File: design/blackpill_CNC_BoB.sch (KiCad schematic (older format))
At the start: 299 parts, among them J101 ALimIN, J102 ZLimIN, J103 YLimIN, J104 XLimIN, J105 CS_IN, J106 FH_IN, J107 DoorIN, J108 ResetIN, J109 ProbeIN, J110 12V Power in, J111 AuxEncIn, J112 5V Power out, J113 ADC_in_1, J114 ADC_in_2, J115 stepDriverLim, J116 Reset, J117 UART1, J118 I2C, J119 SpindleVFD, J120 Spindle/Coolant, J121 Spindle, J122 Coolant, J123 AuxOut, J124 XStepDrv, J125 YStepDrv, J126 ZStepDrv, J127 AStepDrv, U101 TLP290-4, U102 TLP290-4, U103 TLP290-4, U104 74LVC2G17, U105 LD1117S50TR_SOT223, U106 LM358, U107 TLV9001, U108 TLV9001, U109 YAAJ_WeAct_BlackPill_Part_Like, U110 TLV9001, U111 TLV9001, U112 74HCT541, U113 74HCT541, U114 74HCT541, U115 ULN2003A, U116 ULN2003A, U117 ULN2003A

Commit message: place buffer cercos
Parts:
- added C124, C125, C126: 100nF, Capacitor_SMD:C_0603_1608Metric, symbol Device:C
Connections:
- net +5V: now also C125.1
- net GND: now also C124.2, C125.2, C126.2
- net UADCdriver: now also C124.1, C126.1
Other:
- moved on the sheet: C108, C109, C110, C113, JP112
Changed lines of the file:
@@
-$EndComp
-$Comp
-L power:GND #PWR0118
-U 1 1 7569D2D7
-P 4700 10700
-F 0 "#PWR0118" H 4700 10450 50  0001 C CNN
-F 1 "GND" H 4750 10500 50  0001 C CNN
-F 2 "" H 4700 10700 50  0001 C CNN
-F 3 "" H 4700 10700 50  0001 C CNN
-	1    4700 10700
-	1    0    0    -1
-$EndComp
-$Comp
-L Device:C C108
-U 1 1 7569D2E3
-P 4550 10400
-F 0 "C108" H 4600 10300 50  0000 L CNN
-F 1 "100nF" H 4450 10500 50  0000 L CNN
-F 2 "Capacitor_SMD:C_0603_1608Metric" H 4588 10250 50  0001 C CNN
-F 3 "~" H 4550 10400 50  0001 C CNN
-	1    4550 10400
-	1    0    0    -1
-$EndComp
-Wire Wire Line
-	4550 10100 4550 10250
-Wire Wire Line
-	4550 10550 4550 10700
-Wire Wire Line
-	4550 10700 4700 10700
-Wire Wire Line
-	4700 10700 4850 10700
-Connection ~ 4700 10700
-$Comp
-L power:GND #PWR0127
-U 1 1 756F2E58
-P 5450 10700
-F 0 "#PWR0127" H 5450 10450 50  0001 C CNN
-F 1 "GND" H 5500 10500 50  0001 C CNN
-F 2 "" H 5450 10700 50  0001 C CNN
-F 3 "" H 5450 10700 50  0001 C CNN
-	1    5450 10700
-	1    0    0    -1
-$EndComp
-$Comp
-L Device:C C110
-U 1 1 756F2E64
-P 5300 10400
-F 0 "C110" H 5350 10300 50  0000 L CNN
-F 1 "100nF" H 5200 10500 50  0000 L CNN
-F 2 "Capacitor_SMD:C_0603_1608Metric" H 5338 10250 50  0001 C CNN
-F 3 "~" H 5300 10400 50  0001 C CNN
-	1    5300 10400
-	1    0    0    -1
-$EndComp
-Wire Wire Line
-	5300 10100 5300 10250
-Wire Wire Line
-	5300 10550 5300 10700
-Wire Wire Line
-	5300 10700 5450 10700
-Wire Wire Line
-	5450 10700 5600 10700
-Connection ~ 5450 10700
-Wire Wire Line
-	4550 10100 4700 10100
-$Comp
-L power:+5V #PWR0117
-U 1 1 73BC8B53
-P 4700 10100
-F 0 "#PWR0117" H 4700 9950 50  0001 C CNN
-F 1 "+5V" H 4750 10300 50  0001 C CNN
-F 2 "" H 4700 10100 50  0001 C CNN
-F 3 "" H 4700 10100 50  0001 C CNN
-	1    4700 10100
-	1    0    0    -1
-$EndComp
-Connection ~ 4700 10100
-Wire Wire Line
-	4700 10100 4850 10100
-$Comp
-L power:+5V #PWR0125
-U 1 1 758539CE
-P 5350 9500
-F 0 "#PWR0125" H 5350 9350 50  0001 C CNN
-F 1 "+5V" H 5400 9700 50  0001 C CNN
-F 2 "" H 5350 9500 50  0001 C CNN
-F 3 "" H 5350 9500 50  0001 C CNN
-	1    5350 9500
-	0    -1   -1   0
 $EndComp
 $Comp
@@
 Text Label 8150 4600 0    50   ~ 0
 UADCdriver
-$Comp
-L Device:C C109
-U 1 1 768A9165
-P 4850 10400
-F 0 "C109" H 4900 10300 50  0000 L CNN
-F 1 "100nF" H 4750 10500 50  0000 L CNN
-F 2 "Capacitor_SMD:C_0603_1608Metric" H 4888 10250 50  0001 C CNN
-F 3 "~" H 4850 10400 50  0001 C CNN
-	1    4850 10400
-	1    0    0    -1
-$EndComp
-$Comp
-L Device:C C113
-U 1 1 768A9343
-P 5600 10400
-F 0 "C113" H 5650 10300 50  0000 L CNN
-F 1 "100nF" H 5500 10500 50  0000 L CNN
-F 2 "Capacitor_SMD:C_0603_1608Metric" H 5638 10250 50  0001 C CNN
-F 3 "~" H 5600 10400 50  0001 C CNN
-	1    5600 10400
-	1    0    0    -1
-$EndComp
-$Comp
-L power:+3.3V #PWR0126
-U 1 1 768B85AD
-P 5350 10000
-F 0 "#PWR0126" H 5350 9850 50  0001 C CNN
-F 1 "+3.3V" H 5365 10173 50  0001 C CNN
-F 2 "" H 5350 10000 50  0001 C CNN
-F 3 "" H 5350 10000 50  0001 C CNN
-	1    5350 10000
-	0    -1   -1   0
-$EndComp
 Text Label 10700 9600 1    50   ~ 0
 UADCdriver
-Wire Wire Line
-	4850 10100 4850 10250
-Wire Wire Line
-	4850 10550 4850 10700
-Wire Wire Line
-	5600 10700 5600 10550
-Wire Wire Line
-	5600 10100 5600 10250
-$Comp
-L Device:Jumper_NC_Dual JP112
-U 1 1 76A11CC6
-P 5350 9750
-F 0 "JP112" H 5350 9900 50  0000 L CNN
-F 1 "Jumper_NC_Dual" V 5350 9900 50  0001 L CNN
-F 2 "Connector_PinHeader_2.54mm:PinHeader_1x03_P2.54mm_Vertical" H 5350 9750 50  0001 C CNN
-F 3 "~" H 5350 9750 50  0001 C CNN
-	1    5350 9750
-	0    -1   -1   0
-$EndComp
-Wire Wire Line
-	5300 10100 5600 10100
-Connection ~ 5600 10100
-Wire Wire Line
-	5600 9700 5600 9750
-Wire Wire Line
-	5450 9750 5600 9750
-Connection ~ 5600 9750
-Wire Wire Line
-	5600 9750 5600 10100
 $Comp
 L Device:R R141
@@
 Wire Wire Line
 	2900 10850 3050 10850
-Text Label 5600 9700 0    50   ~ 0
-UADCdriver
 $Comp
 L Diode:1N5819 D120
@@
 Wire Wire Line
 	6240 2980 6110 2980
+Text Label 4800 8900 0    50   ~ 0
+UADCdriver
+Wire Wire Line
+	4800 8950 4800 9300
+Connection ~ 4800 8950
+Wire Wire Line
+	4650 8950 4800 8950
+Wire Wire Line
+	4800 8900 4800 8950
+Connection ~ 4800 9300
+Wire Wire Line
+	4500 9300 4800 9300
+$Comp
+L Device:Jumper_NC_Dual JP112
+U 1 1 76A11CC6
+P 4550 8950
+F 0 "JP112" H 4550 9100 50  0000 L CNN
+F 1 "Jumper_NC_Dual" V 4550 9100 50  0001 L CNN
+F 2 "Connector_PinHeader_2.54mm:PinHeader_1x03_P2.54mm_Vertical" H 4550 8950 50  0001 C CNN
+F 3 "~" H 4550 8950 50  0001 C CNN
+	1    4550 8950
+	0    -1   -1   0
+$EndComp
+Wire Wire Line
+	4800 9300 4800 9450
+Wire Wire Line
+	4800 9900 4800 9750
+$Comp
+L power:+3.3V #PWR0126
+U 1 1 768B85AD
+P 4550 9200
+F 0 "#PWR0126" H 4550 9050 50  0001 C CNN
+F 1 "+3.3V" H 4565 9373 50  0001 C CNN
+F 2 "" H 4550 9200 50  0001 C CNN
+F 3 "" H 4550 9200 50  0001 C CNN
+	1    4550 9200
+	0    -1   -1   0
+$EndComp
+$Comp
+L Device:C C113
+U 1 1 768A9343
+P 4800 9600
+F 0 "C113" H 4850 9500 50  0000 L CNN
+F 1 "100nF" H 4700 9700 50  0000 L CNN
+F 2 "Capacitor_SMD:C_0603_1608Metric" H 4838 9450 50  0001 C CNN
+F 3 "~" H 4800 9600 50  0001 C CNN
+	1    4800 9600
+	1    0    0    -1
+$EndComp
+$Comp
+L power:+5V #PWR0125
+U 1 1 758539CE
+P 4550 8700
+F 0 "#PWR0125" H 4550 8550 50  0001 C CNN
+F 1 "+5V" H 4600 8900 50  0001 C CNN
+F 2 "" H 4550 8700 50  0001 C CNN
+F 3 "" H 4550 8700 50  0001 C CNN
+	1    4550 8700
+	0    -1   -1   0
+$EndComp
+Connection ~ 4650 9900
+Wire Wire Line
+	4650 9900 4800 9900
+Wire Wire Line
+	4500 9900 4650 9900
+Wire Wire Line
+	4500 9750 4500 9900
+Wire Wire Line
+	4500 9300 4500 9450
+$Comp
+L Device:C C110
+U 1 1 756F2E64
+P 4500 9600
+F 0 "C110" H 4550 9500 50  0000 L CNN
+F 1 "100nF" H 4400 9700 50  0000 L CNN
+F 2 "Capacitor_SMD:C_0603_1608Metric" H 4538 9450 50  0001 C CNN
+F 3 "~" H 4500 9600 50  0001 C CNN
+	1    4500 9600
+	1    0    0    -1
+$EndComp
+$Comp
+L power:GND #PWR0127
+U 1 1 756F2E58
+P 4650 9900
+F 0 "#PWR0127" H 4650 9650 50  0001 C CNN
+F 1 "GND" H 4700 9700 50  0001 C CNN
+F 2 "" H 4650 9900 50  0001 C CNN
+F 3 "" H 4650 9900 50  0001 C CNN
+	1    4650 9900
+	1    0    0    -1
+$EndComp
+Wire Wire Line
+	4850 10750 4850 10900
+Wire Wire Line
+	4850 10300 4850 10450
+$Comp
+L Device:C C109
+U 1 1 768A9165
+P 4850 10600
+F 0 "C109" H 4900 10500 50  0000 L CNN
+F 1 "100nF" H 4750 10700 50  0000 L CNN
+F 2 "Capacitor_SMD:C_0603_1608Metric" H 4888 10450 50  0001 C CNN
+F 3 "~" H 4850 10600 50  0001 C CNN
+	1    4850 10600
+	1    0    0    -1
+$EndComp
+Wire Wire Line
+	4700 10300 4850 10300
+Connection ~ 4700 10300
+$Comp
+L power:+5V #PWR0117
+U 1 1 73BC8B53
+P 4700 10300
+F 0 "#PWR0117" H 4700 10150 50  0001 C CNN
+F 1 "+5V" H 4750 10500 50  0001 C CNN
+F 2 "" H 4700 10300 50  0001 C CNN
+F 3 "" H 4700 10300 50  0001 C CNN
+	1    4700 10300
+	1    0    0    -1
+$EndComp
+Wire Wire Line
+	4550 10300 4700 10300
+Connection ~ 4700 10900
+Wire Wire Line
+	4700 10900 4850 10900
+Wire Wire Line
+	4550 10900 4700 10900
+Wire Wire Line
+	4550 10750 4550 10900
+Wire Wire Line
+	4550 10300 4550 10450
+$Comp
+L Device:C C108
+U 1 1 7569D2E3
+P 4550 10600
+F 0 "C108" H 4600 10500 50  0000 L CNN
+F 1 "100nF" H 4450 10700 50  0000 L CNN
+F 2 "Capacitor_SMD:C_0603_1608Metric" H 4588 10450 50  0001 C CNN
+F 3 "~" H 4550 10600 50  0001 C CNN
+	1    4550 10600
+	1    0    0    -1
+$EndComp
+$Comp
+L power:GND #PWR0118
+U 1 1 7569D2D7
+P 4700 10900
+F 0 "#PWR0118" H 4700 10650 50  0001 C CNN
+F 1 "GND" H 4750 10700 50  0001 C CNN
+F 2 "" H 4700 10900 50  0001 C CNN
+F 3 "" H 4700 10900 50  0001 C CNN
+	1    4700 10900
+	1    0    0    -1
+$EndComp
+$Comp
+L Device:C C125
+U 1 1 68D74ED4
+P 5100 10600
+F 0 "C125" H 5150 10500 50  0000 L CNN
+F 1 "100nF" H 5000 10700 50  0000 L CNN
+F 2 "Capacitor_SMD:C_0603_1608Metric" H 5138 10450 50  0001 C CNN
+F 3 "~" H 5100 10600 50  0001 C CNN
+	1    5100 10600
+	1    0    0    -1
+$EndComp
+$Comp
+L Device:C C124
+U 1 1 68E10737
+P 5100 9600
+F 0 "C124" H 5150 9500 50  0000 L CNN
+F 1 "100nF" H 5000 9700 50  0000 L CNN
+F 2 "Capacitor_SMD:C_0603_1608Metric" H 5138 9450 50  0001 C CNN
+F 3 "~" H 5100 9600 50  0001 C CNN
+	1    5100 9600
+	1    0    0    -1
+$EndComp
+$Comp
+L Device:C C126
+U 1 1 68E11AD2
+P 5400 9600
+F 0 "C126" H 5450 9500 50  0000 L CNN
+F 1 "100nF" H 5300 9700 50  0000 L CNN
+F 2 "Capacitor_SMD:C_0603_1608Metric" H 5438 9450 50  0001 C CNN
+F 3 "~" H 5400 9600 50  0001 C CNN
+	1    5400 9600
+	1    0    0    -1
+$EndComp
+Wire Wire Line
+	4850 10300 5100 10300
+Wire Wire Line
+	5100 10300 5100 10450
+Connection ~ 4850 10300
+Wire Wire Line
+	4850 10900 5100 10900
+Wire Wire Line
+	5100 10900 5100 10750
+Connection ~ 4850 10900
+Wire Wire Line
+	4800 9900 5100 9900
+Wire Wire Line
+	5400 9900 5400 9750
+Connection ~ 4800 9900
+Wire Wire Line
+	5100 9750 5100 9900
+Connection ~ 5100 9900
+Wire Wire Line
+	5100 9900 5400 9900
+Wire Wire Line
+	4800 9300 5100 9300
+Wire Wire Line
+	5400 9300 5400 9450
+Wire Wire Line
+	5100 9450 5100 9300
+Connection ~ 5100 9300
+Wire Wire Line
+	5100 9300 5400 9300
 $EndSCHEMATC

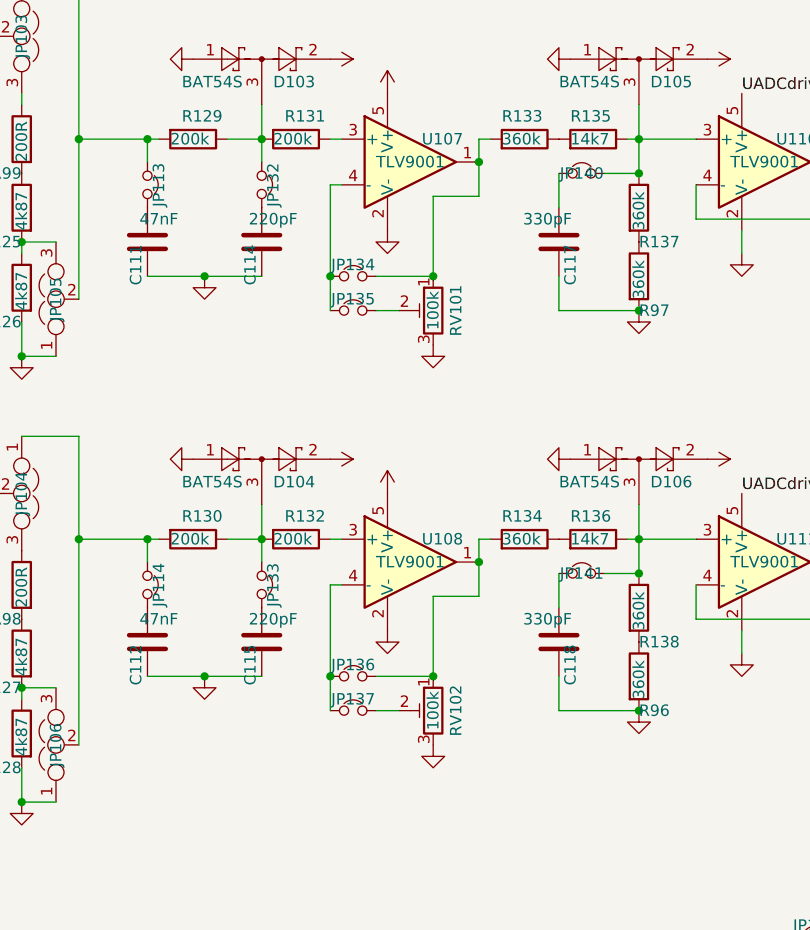
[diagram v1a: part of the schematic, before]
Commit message: refigure AD in jumper
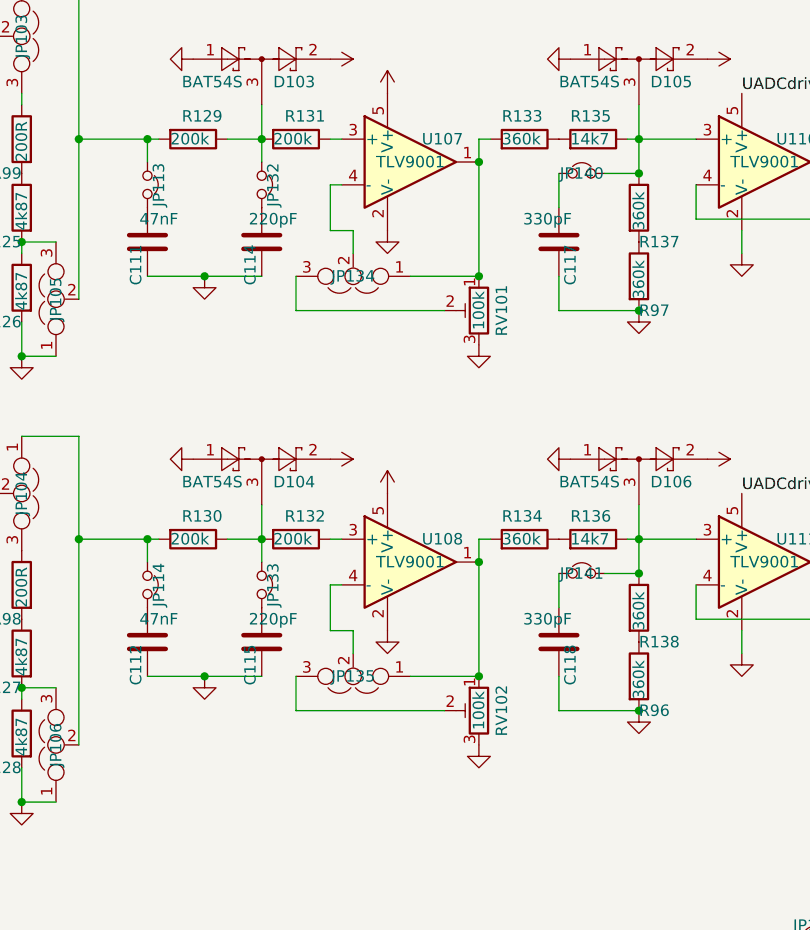
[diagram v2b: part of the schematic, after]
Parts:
- removed JP134, JP135, JP136, JP137: Jumper_NC_Small, Connector_PinHeader_2.54mm:PinHeader_1x02_P2.54mm_Vertical, symbol Device:Jumper_NC_Small
- added JP134, JP135: Jumper_NC_Dual, Connector_PinHeader_2.54mm:PinHeader_1x03_P2.54mm_Vertical, symbol Device:Jumper_NC_Dual
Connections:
- net at R133.2, RV101.1, U107.1: now also JP134.1
- net at RV101.2: now also JP134.3
- net at U107.4 (-): now also JP134.2
- net at R134.2, RV102.1, U108.1: now also JP135.1
- net at RV102.2: now also JP135.3
- net at U108.4 (-): now also JP135.2
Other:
- moved on the sheet: RV101, RV102
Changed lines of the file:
@@
 L Device:R_POT_TRIM RV101
 U 1 1 74D34F66
-P 6800 5550
-F 0 "RV101" V 6700 5550 50  0000 C CNN
-F 1 "100k" V 6800 5550 50  0000 C CNN
-F 2 "Potentiometer_THT:Potentiometer_Bourns_3296W_Vertical" H 6800 5550 50  0001 C CNN
-F 3 "~" H 6800 5550 50  0001 C CNN
-	1    6800 5550
+P 7000 5550
+F 0 "RV101" V 6900 5550 50  0000 C CNN
+F 1 "100k" V 7000 5550 50  0000 C CNN
+F 2 "Potentiometer_THT:Potentiometer_Bourns_3296W_Vertical" H 7000 5550 50  0001 C CNN
+F 3 "~" H 7000 5550 50  0001 C CNN
+	1    7000 5550
 	-1   0    0    -1
 $EndComp
@@
 L power:GNDS #PWR0143
 U 1 1 74FB2393
-P 6800 5700
-F 0 "#PWR0143" H 6800 5450 50  0001 C CNN
-F 1 "GNDS" H 6805 5527 50  0001 C CNN
-F 2 "" H 6800 5700 50  0001 C CNN
-F 3 "" H 6800 5700 50  0001 C CNN
-	1    6800 5700
-	1    0    0    -1
-$EndComp
-$Comp
-L Device:Jumper_NC_Small JP135
-U 1 1 74FB28D6
-P 6450 5550
-F 0 "JP135" H 6450 5600 50  0000 C CNN
-F 1 "Jumper_NC_Small" H 6450 5700 50  0001 C CNN
-F 2 "Connector_PinHeader_2.54mm:PinHeader_1x02_P2.54mm_Vertical" H 6450 5550 50  0001 C CNN
-F 3 "~" H 6450 5550 50  0001 C CNN
-	1    6450 5550
-	-1   0    0    -1
-$EndComp
-$Comp
-L Device:Jumper_NC_Small JP134
-U 1 1 74FB2AFA
-P 6450 5400
-F 0 "JP134" H 6450 5450 50  0000 C CNN
-F 1 "Jumper_NC_Small" H 6450 5550 50  0001 C CNN
-F 2 "Connector_PinHeader_2.54mm:PinHeader_1x02_P2.54mm_Vertical" H 6450 5400 50  0001 C CNN
-F 3 "~" H 6450 5400 50  0001 C CNN
-	1    6450 5400
-	-1   0    0    -1
+P 7000 5700
+F 0 "#PWR0143" H 7000 5450 50  0001 C CNN
+F 1 "GNDS" H 7005 5527 50  0001 C CNN
+F 2 "" H 7000 5700 50  0001 C CNN
+F 3 "" H 7000 5700 50  0001 C CNN
+	1    7000 5700
+	1    0    0    -1
 $EndComp
 $Comp
@@
 $EndComp
 Wire Wire Line
-	6350 5550 6350 5400
-Wire Wire Line
 	6350 5000 6400 5000
-Connection ~ 6350 5400
-Wire Wire Line
-	6350 5400 6350 5000
-Wire Wire Line
-	6550 5400 6800 5400
-Wire Wire Line
-	6650 5550 6550 5550
-Wire Wire Line
-	7000 4900 7000 5050
-Wire Wire Line
-	7000 5050 6800 5050
-Wire Wire Line
-	6800 5050 6800 5400
-Connection ~ 6800 5400
 $Comp
 L Device:R R135
@@
 L Device:R_POT_TRIM RV102
 U 1 1 77513692
-P 6800 7300
-F 0 "RV102" V 6700 7300 50  0000 C CNN
-F 1 "100k" V 6800 7300 50  0000 C CNN
-F 2 "Potentiometer_THT:Potentiometer_Bourns_3296W_Vertical" H 6800 7300 50  0001 C CNN
-F 3 "~" H 6800 7300 50  0001 C CNN
-	1    6800 7300
+P 7000 7300
+F 0 "RV102" V 6900 7300 50  0000 C CNN
+F 1 "100k" V 7000 7300 50  0000 C CNN
+F 2 "Potentiometer_THT:Potentiometer_Bourns_3296W_Vertical" H 7000 7300 50  0001 C CNN
+F 3 "~" H 7000 7300 50  0001 C CNN
+	1    7000 7300
 	-1   0    0    -1
 $EndComp
@@
 L power:GNDS #PWR0144
 U 1 1 77513698
-P 6800 7450
-F 0 "#PWR0144" H 6800 7200 50  0001 C CNN
-F 1 "GNDS" H 6805 7277 50  0001 C CNN
-F 2 "" H 6800 7450 50  0001 C CNN
-F 3 "" H 6800 7450 50  0001 C CNN
-	1    6800 7450
-	1    0    0    -1
-$EndComp
-$Comp
-L Device:Jumper_NC_Small JP137
-U 1 1 7751369E
-P 6450 7300
-F 0 "JP137" H 6450 7350 50  0000 C CNN
-F 1 "Jumper_NC_Small" H 6450 7450 50  0001 C CNN
-F 2 "Connector_PinHeader_2.54mm:PinHeader_1x02_P2.54mm_Vertical" H 6450 7300 50  0001 C CNN
-F 3 "~" H 6450 7300 50  0001 C CNN
-	1    6450 7300
-	-1   0    0    -1
-$EndComp
-$Comp
-L Device:Jumper_NC_Small JP136
-U 1 1 775136A4
-P 6450 7150
-F 0 "JP136" H 6450 7200 50  0000 C CNN
-F 1 "Jumper_NC_Small" H 6450 7300 50  0001 C CNN
-F 2 "Connector_PinHeader_2.54mm:PinHeader_1x02_P2.54mm_Vertical" H 6450 7150 50  0001 C CNN
-F 3 "~" H 6450 7150 50  0001 C CNN
-	1    6450 7150
-	-1   0    0    -1
+P 7000 7450
+F 0 "#PWR0144" H 7000 7200 50  0001 C CNN
+F 1 "GNDS" H 7005 7277 50  0001 C CNN
+F 2 "" H 7000 7450 50  0001 C CNN
+F 3 "" H 7000 7450 50  0001 C CNN
+	1    7000 7450
+	1    0    0    -1
 $EndComp
 $Comp
@@
 $EndComp
 Wire Wire Line
-	6350 7300 6350 7150
-Wire Wire Line
 	6350 6750 6400 6750
-Connection ~ 6350 7150
-Wire Wire Line
-	6350 7150 6350 6750
-Wire Wire Line
-	6550 7150 6800 7150
-Wire Wire Line
-	6650 7300 6550 7300
-Wire Wire Line
-	7000 6650 7000 6800
-Wire Wire Line
-	7000 6800 6800 6800
-Wire Wire Line
-	6800 6800 6800 7150
-Connection ~ 6800 7150
 $Comp
 L Device:R R136
@@
 Wire Wire Line
 	5100 9300 5400 9300
+$Comp
+L Device:Jumper_NC_Dual JP135
+U 1 1 6913274A
+P 6450 7150
+F 0 "JP135" H 6450 7150 50  0000 C CNN
+F 1 "Jumper_NC_Dual" H 6450 7350 50  0001 C CNN
+F 2 "Connector_PinHeader_2.54mm:PinHeader_1x03_P2.54mm_Vertical" H 6450 7150 50  0001 C CNN
+F 3 "~" H 6450 7150 50  0001 C CNN
+	1    6450 7150
+	-1   0    0    1
+$EndComp
+$Comp
+L Device:Jumper_NC_Dual JP134
+U 1 1 6913117A
+P 6450 5400
+F 0 "JP134" H 6450 5400 50  0000 C CNN
+F 1 "Jumper_NC_Dual" H 6450 5600 50  0001 C CNN
+F 2 "Connector_PinHeader_2.54mm:PinHeader_1x03_P2.54mm_Vertical" H 6450 5400 50  0001 C CNN
+F 3 "~" H 6450 5400 50  0001 C CNN
+	1    6450 5400
+	-1   0    0    1
+$EndComp
+Wire Wire Line
+	6850 5550 6200 5550
+Wire Wire Line
+	6200 5550 6200 5400
+Wire Wire Line
+	6700 5400 7000 5400
+Wire Wire Line
+	7000 4900 7000 5400
+Connection ~ 7000 5400
+Wire Wire Line
+	6450 5300 6450 5200
+Wire Wire Line
+	6450 5200 6350 5200
+Wire Wire Line
+	6350 5200 6350 5000
+Wire Wire Line
+	7000 6650 7000 7150
+Wire Wire Line
+	7000 7150 6700 7150
+Connection ~ 7000 7150
+Wire Wire Line
+	6200 7150 6200 7300
+Wire Wire Line
+	6200 7300 6850 7300
+Wire Wire Line
+	6450 7050 6450 6950
+Wire Wire Line
+	6450 6950 6350 6950
+Wire Wire Line
+	6350 6950 6350 6750
 $EndSCHEMATC

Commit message: refigure driver voltage jumper
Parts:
- added J128: Driver Power in/out, Connector_Phoenix_MSTB:PhoenixContact_MSTBA_2,5_2-G-5,08_1x02_P5.08mm_Horizontal, symbol Connector:Screw_Terminal_01x02
- added JP136: Jumper_NC_Dual, Connector_PinHeader_2.54mm:PinHeader_1x03_P2.54mm_Vertical, symbol Device:Jumper_NC_Dual
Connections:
- net +12V: now also JP136.3
- net +5V: now also JP136.1
- net GND: now also J128.1 (Pin_1)
- net Vdrive: now also J128.2 (Pin_2), JP136.2
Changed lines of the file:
@@
 Wire Wire Line
 	6350 6950 6350 6750
+$Comp
+L Nucleo64-CNC-rescue:Vdrive-power #PWR0132
+U 1 1 698A2D21
+P 6950 8950
+F 0 "#PWR0132" H 6750 8800 50  0001 C CNN
+F 1 "Vdrive" H 6967 9123 50  0000 C CNN
+F 2 "" H 6950 8950 50  0001 C CNN
+F 3 "" H 6950 8950 50  0001 C CNN
+	1    6950 8950
+	1    0    0    -1
+$EndComp
+$Comp
+L Connector:Screw_Terminal_01x02 J128
+U 1 1 698AEEDC
+P 7150 9300
+F 0 "J128" H 7150 9100 50  0000 C CNN
+F 1 "Driver Power in/out" V 7300 9250 50  0000 C CNN
+F 2 "Connector_Phoenix_MSTB:PhoenixContact_MSTBA_2,5_2-G-5,08_1x02_P5.08mm_Horizontal" H 7150 9300 50  0001 C CNN
+F 3 "~" H 7150 9300 50  0001 C CNN
+	1    7150 9300
+	1    0    0    1
+$EndComp
+$Comp
+L power:GND #PWR0152
+U 1 1 698B07EF
+P 6950 9300
+F 0 "#PWR0152" H 6950 9050 50  0001 C CNN
+F 1 "GND" H 7000 9100 50  0001 C CNN
+F 2 "" H 6950 9300 50  0001 C CNN
+F 3 "" H 6950 9300 50  0001 C CNN
+	1    6950 9300
+	1    0    0    -1
+$EndComp
+$Comp
+L Device:Jumper_NC_Dual JP136
+U 1 1 698B1E24
+P 6750 9200
+F 0 "JP136" H 6750 9350 50  0000 L CNN
+F 1 "Jumper_NC_Dual" V 6750 9350 50  0001 L CNN
+F 2 "Connector_PinHeader_2.54mm:PinHeader_1x03_P2.54mm_Vertical" H 6750 9200 50  0001 C CNN
+F 3 "~" H 6750 9200 50  0001 C CNN
+	1    6750 9200
+	0    -1   -1   0
+$EndComp
+$Comp
+L power:+5V #PWR0203
+U 1 1 698C5FFC
+P 6750 9450
+F 0 "#PWR0203" H 6750 9300 50  0001 C CNN
+F 1 "+5V" V 6750 9650 50  0000 C CNN
+F 2 "" H 6750 9450 50  0001 C CNN
+F 3 "" H 6750 9450 50  0001 C CNN
+	1    6750 9450
+	0    -1   -1   0
+$EndComp
+$Comp
+L power:+12V #PWR0204
+U 1 1 698CEBA8
+P 6750 8950
+F 0 "#PWR0204" H 6750 8800 50  0001 C CNN
+F 1 "+12V" V 6750 9200 50  0000 C CNN
+F 2 "" H 6750 8950 50  0001 C CNN
+F 3 "" H 6750 8950 50  0001 C CNN
+	1    6750 8950
+	0    -1   1    0
+$EndComp
+Wire Wire Line
+	6850 9200 6950 9200
+Wire Wire Line
+	6950 9200 6950 8950
+Connection ~ 6950 9200
 $EndSCHEMATC
